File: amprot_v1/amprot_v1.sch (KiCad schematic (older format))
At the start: 54 parts, among them J1 ISP, J10 SPEAKER-, J11 SPEAKER+, J12 B+, J13 GND, J14 V+ (12V), J2 V+ (12V), J3 GND, J4 B+, J5 B-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

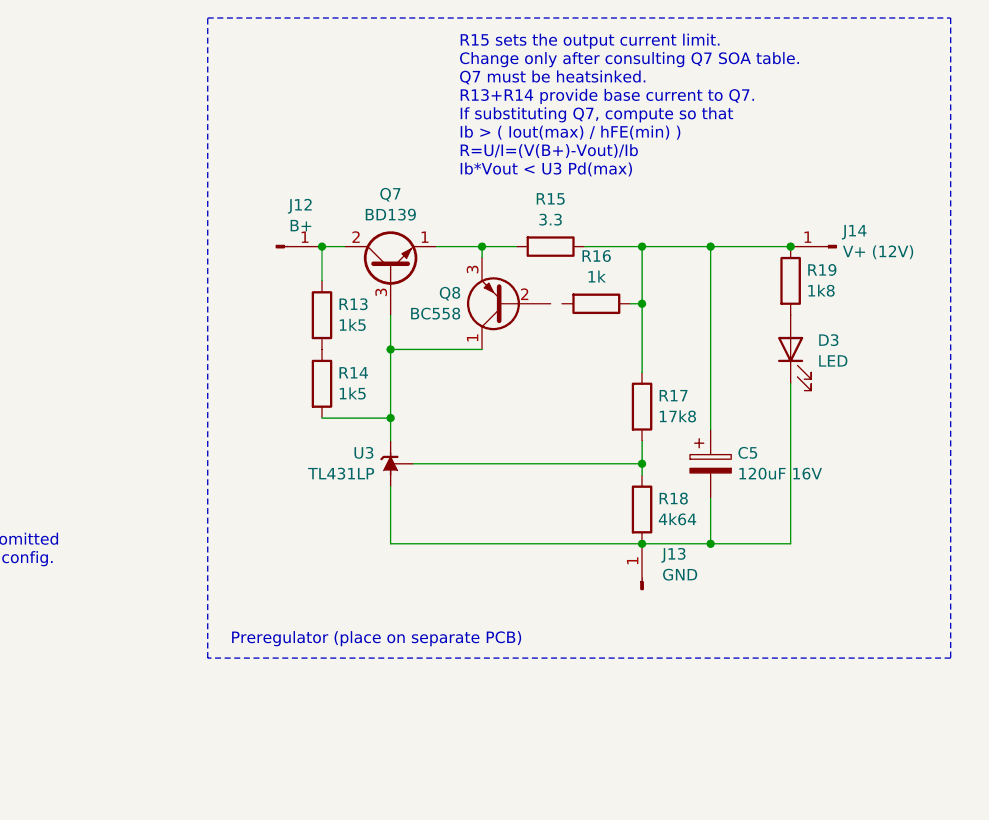
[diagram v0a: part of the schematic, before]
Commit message: Fix errors in schematic
Q8 B was not connected. Add note on B+ max voltage and V+ max current.
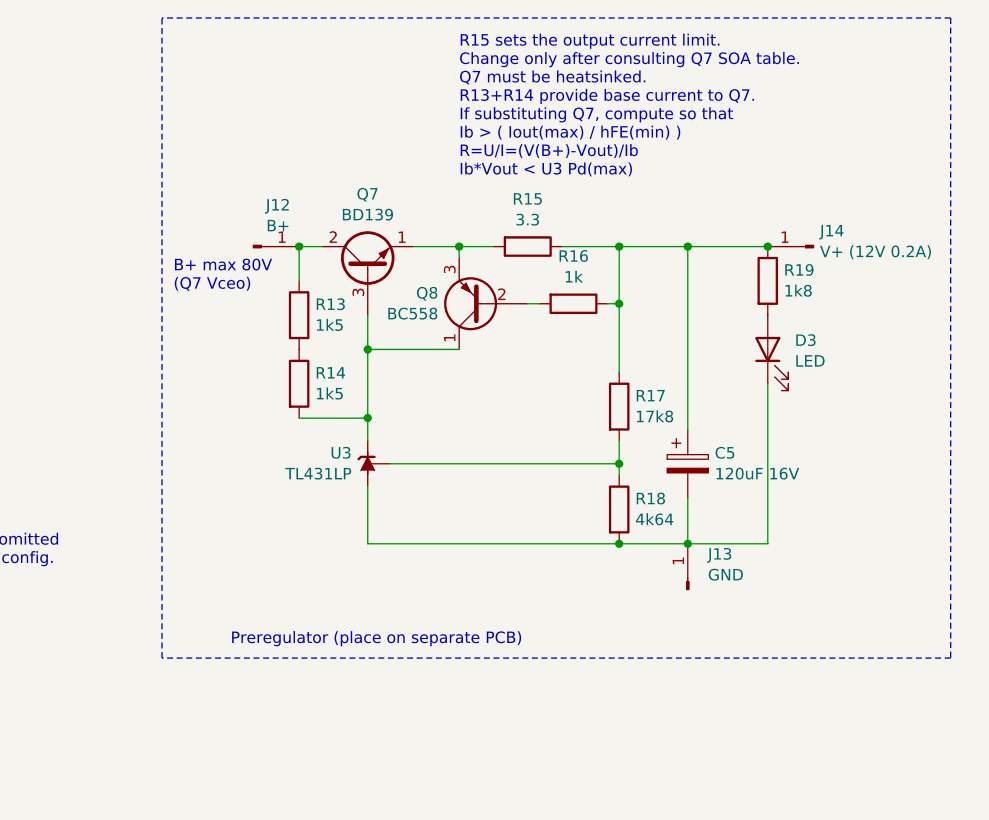
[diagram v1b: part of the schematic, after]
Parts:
- J14: value V+ (12V) -> V+ (12V 0.2A)
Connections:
- net at Q8.2 (B): now also R16.2
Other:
- note added: "B+ max 80V\n(Q7 Vceo)"
- moved on the sheet: C5, D3, J12, J13, J14, Q7, Q8, R13, R14, R15, R16, R17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

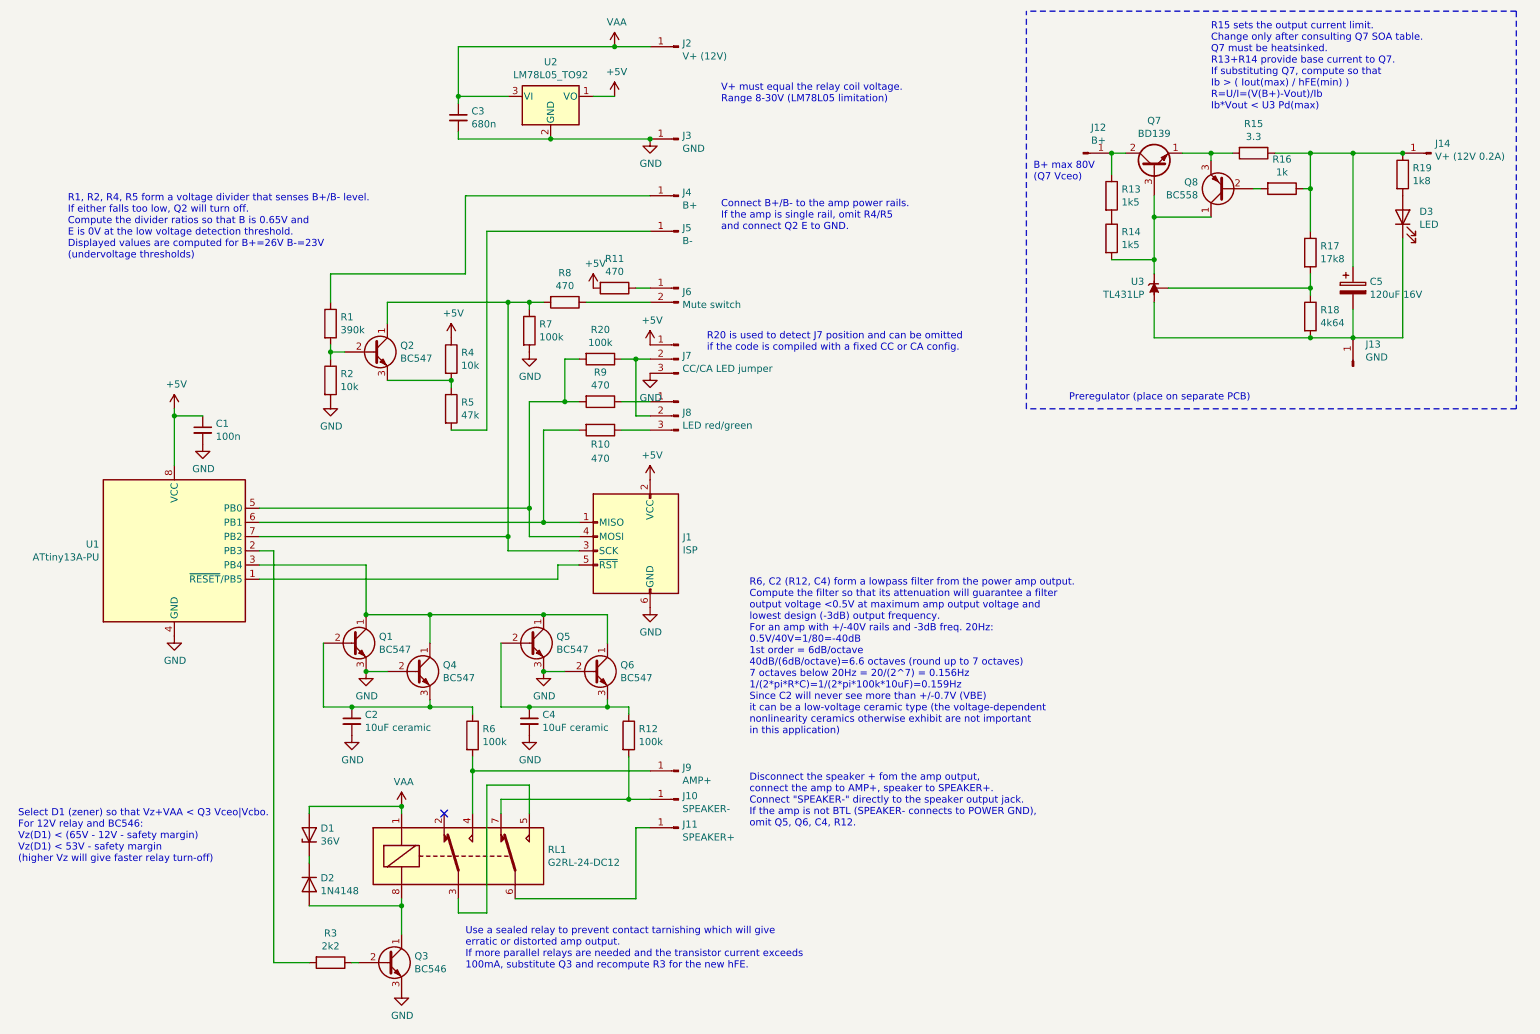
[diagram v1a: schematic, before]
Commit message: Add missing NTC and pullup
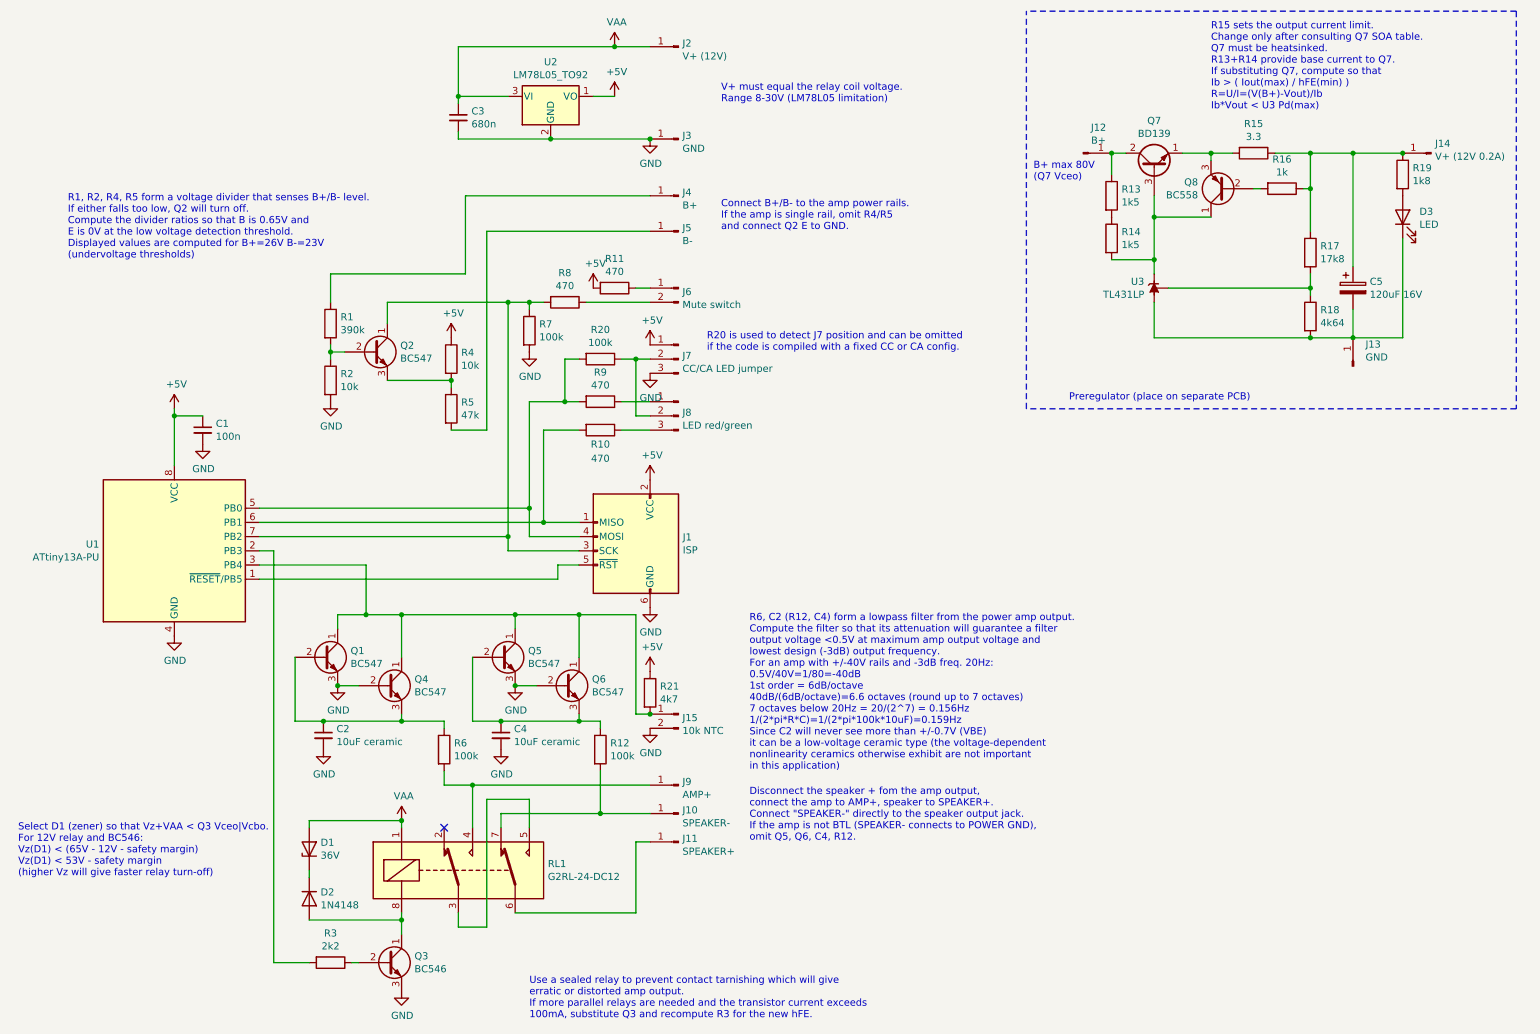
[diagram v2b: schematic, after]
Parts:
- added J15: 10k NTC, symbol Connector:Conn_01x02_Male
- added R21: 4k7, symbol Device:R
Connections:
- net +5V: now also R21.1
- net GND: now also J15.2 (Pin_2)
- net at Q1.1 (C), Q4.1 (C), Q5.1 (C)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: now also J15.1 (Pin_1), R21.2
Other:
- moved on the sheet: C2, C4, D1, D2, J10, J11, J9, Q1, Q4, Q5, Q6, R12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
